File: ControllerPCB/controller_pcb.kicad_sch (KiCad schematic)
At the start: 10 parts, among them U1 Pico, U3 AP63203WU

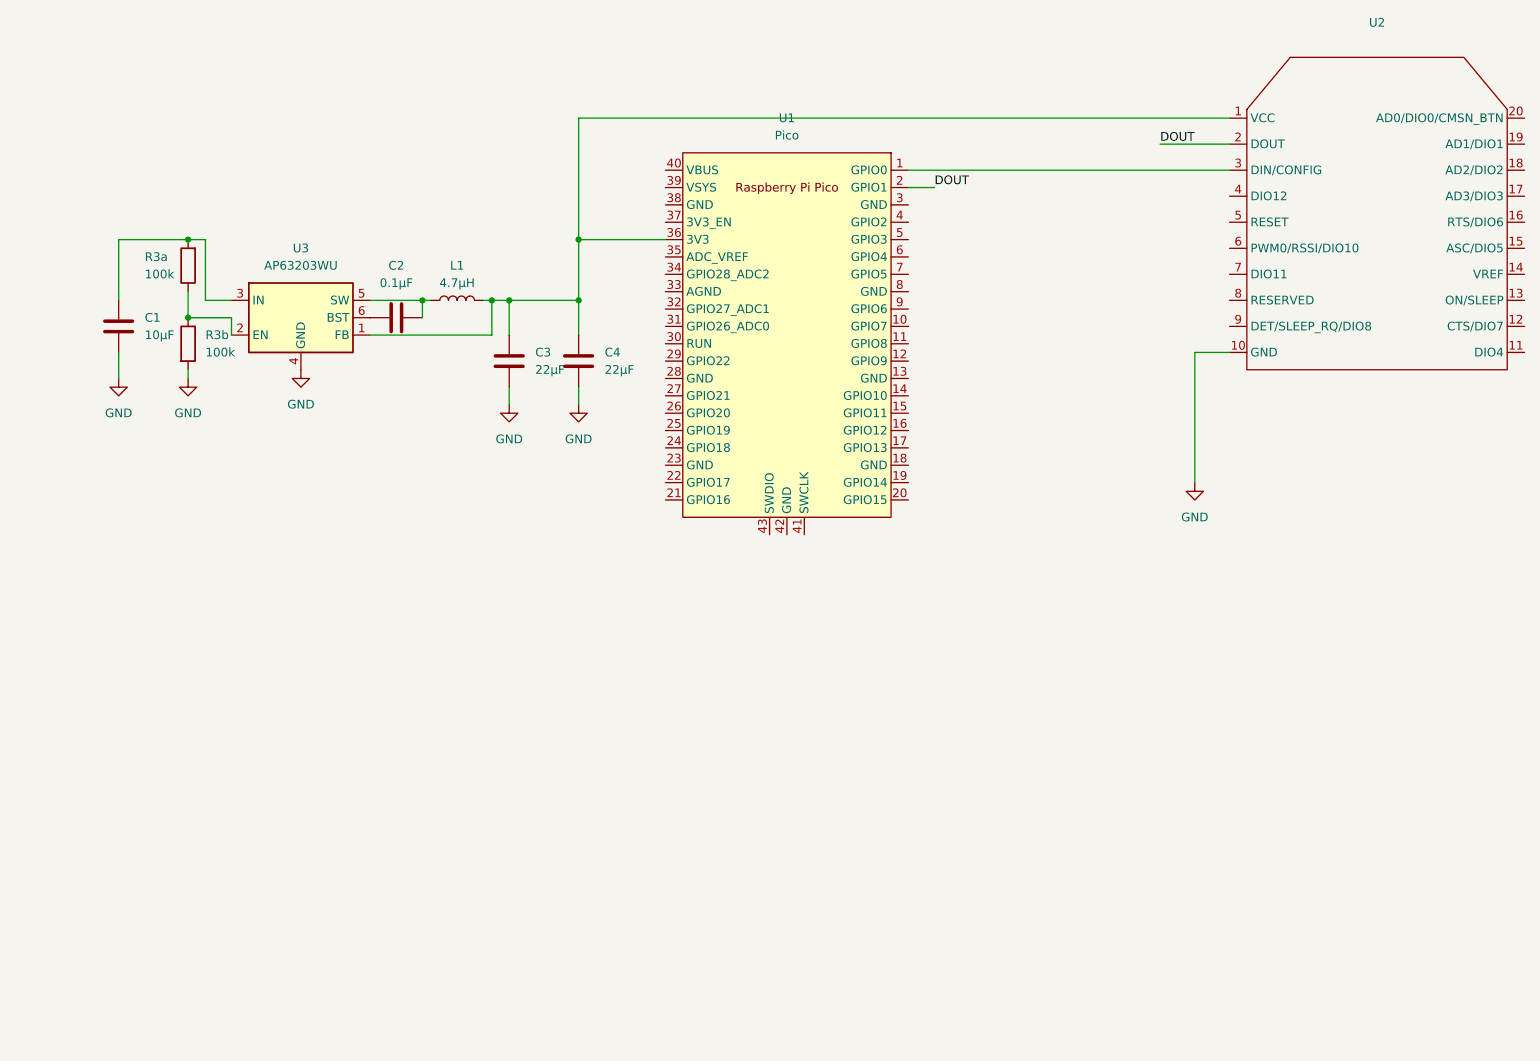
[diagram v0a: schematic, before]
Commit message: Added USB-C headers
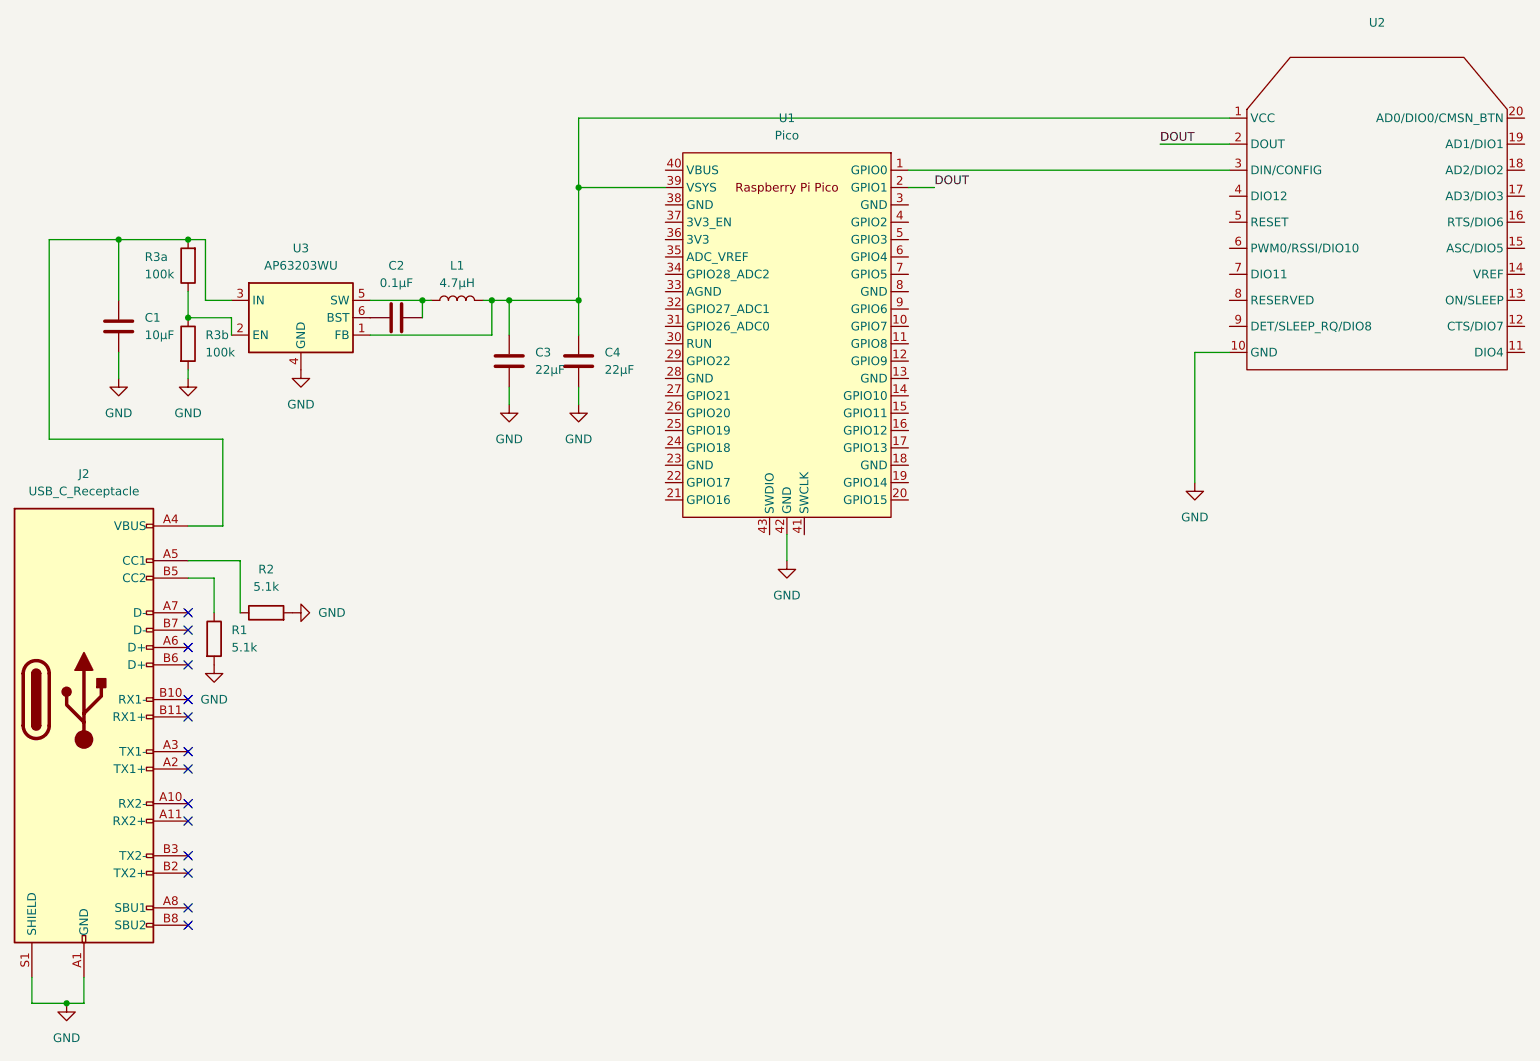
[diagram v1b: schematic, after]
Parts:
- added J2: USB_C_Receptacle, symbol Connector:USB_C_Receptacle
- added R1, R2: 5.1k, Resistor_SMD:R_0603_1608Metric, symbol Device:R
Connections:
- net GND: now also U1.42 (GND), J2.A1 (GND), J2.A12 (GND), J2.B1 (GND), J2.B12 (GND), J2.S1 (SHIELD), R1.2, R2.2
- net at C3.1, C4.1, L1.2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: now also U1.39 (VSYS); no longer U1.36 (3V3)
- net at C1.1, R3a.2, U3.3 (IN): now also J2.A4 (VBUS), J2.A9 (VBUS), J2.B4 (VBUS), J2.B9 (VBUS)
- new net: J2.B5 (CC2), R1.1
- new net: J2.A5 (CC1), R2.1
- no-connect marks 0 -> 14

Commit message: MVP - FIles
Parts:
- removed C1: 10µF, symbol Device:C
- removed C2: 0.1µF, symbol Device:C
- removed C3, C4: 22µF, symbol Device:C
- removed J2: USB_C_Receptacle, symbol Connector:USB_C_Receptacle
- removed L1: 4.7µH, symbol Device:L
- removed R1, R2: 5.1k, Resistor_SMD:R_0603_1608Metric, symbol Device:R
- removed R3a, R3b: 100k, symbol Device:R
- removed U3: AP63203WU, Package_TO_SOT_SMD:TSOT-23-6, symbol Regulator_Switching:AP63203WU
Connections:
- net GND: no longer U1.42 (GND)
- net at U1.39 (VSYS): no longer U2.1 (VCC)
- no-connect marks 14 -> 0

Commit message: Add files via upload
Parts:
- added C1: 10µF, symbol Device:C
- added C2: 0.1µF, symbol Device:C
- added C3, C4: 22µF, symbol Device:C
- added L1: 4.7µH, symbol Device:L
- added R3a, R3b: 100k, symbol Device:R
- added U3: AP63203WU, Package_TO_SOT_SMD:TSOT-23-6, symbol Regulator_Switching:AP63203WU
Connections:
- net GND: now also C1.2, C3.2, C4.2, R3b.2, U3.4 (GND)
- net at U1.36 (3V3): now also U2.1 (VCC), C3.1, C4.1, L1.2, U3.1 (FB)
- new net: C2.2, L1.1, U3.5 (SW)
- new net: R3a.1, R3b.1, U3.2 (EN)
- new net: C1.1, R3a.2, U3.3 (IN)
- new net: C2.1, U3.6 (BST)
